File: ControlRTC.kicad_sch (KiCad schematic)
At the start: 28 parts, among them M1 Fan_4pin, SW1 SW_USER, SW2 SW_WIPE, U18 74LVC1G07, U19 74LVC1G07, U20 LP5569RTWR, U21 PCF85063AT, Y2 X32K768S301

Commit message: Use impedance for JLC7628 stackup/switch HDMI/SW2 placement
Use JLC7628 impedance values to get more options in color selection.
Also this leads to slightly wider traces typically, and it will be
easier to switch back to JLC2313 or the like than the other way around.

Also swap placing of HDMI/SW2 and rotate the heatsink by 90° for easier
routing.

Signed-off-by: Stefan Agner <stefan@agner.ch>
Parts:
- SW1: footprint Button_Switch_THT:SW_Tactile_SPST_Angled_PTS645Vx58-2LFS -> Button_Switch_THT:SW_Tactile_SPST_Angled_PTS645Vx83-2LFS; PartNumber PTS645VM58-2 LFS -> PTS645VM83-2 LFS
- SW2: footprint Button_Switch_THT:SW_Tactile_SPST_Angled_PTS645Vx39-2LFS -> Button_Switch_THT:SW_Tactile_SPST_Angled_PTS645Vx58-2LFS; PartNumber PTS645VK39-2 LFS -> PTS645VK58-2 LFS
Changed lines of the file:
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@@
     (property "Reference" "SW1" (id 0) (at 60.325 39.37 0))
     (property "Value" "SW_USER" (id 1) (at 60.325 41.91 0))
-    (property "Footprint" "Button_Switch_THT:SW_Tactile_SPST_Angled_PTS645Vx58-2LFS" (id 2) (at 59.69 46.355 0)
+    (property "Footprint" "Button_Switch_THT:SW_Tactile_SPST_Angled_PTS645Vx83-2LFS" (id 2) (at 59.69 46.355 0)
       (effects (font (size 1.27 1.27)) hide)
     )
@@
       (effects (font (size 1.27 1.27)) hide)
     )
-    (property "PartNumber" "PTS645VM58-2 LFS" (id 5) (at 59.69 46.355 0)
+    (property "PartNumber" "PTS645VM83-2 LFS" (id 5) (at 59.69 46.355 0)
       (effects (font (size 1.27 1.27)) hide)
     )
@@
     (property "Reference" "SW2" (id 0) (at 102.235 39.37 0))
     (property "Value" "SW_WIPE" (id 1) (at 102.235 41.91 0))
-    (property "Footprint" "Button_Switch_THT:SW_Tactile_SPST_Angled_PTS645Vx39-2LFS" (id 2) (at 101.6 46.355 0)
+    (property "Footprint" "Button_Switch_THT:SW_Tactile_SPST_Angled_PTS645Vx58-2LFS" (id 2) (at 101.6 46.355 0)
       (effects (font (size 1.27 1.27)) hide)
     )
@@
       (effects (font (size 1.27 1.27)) hide)
     )
-    (property "PartNumber" "PTS645VK39-2 LFS" (id 5) (at 101.6 46.355 0)
+    (property "PartNumber" "PTS645VK58-2 LFS" (id 5) (at 101.6 46.355 0)
       (effects (font (size 1.27 1.27)) hide)
     )

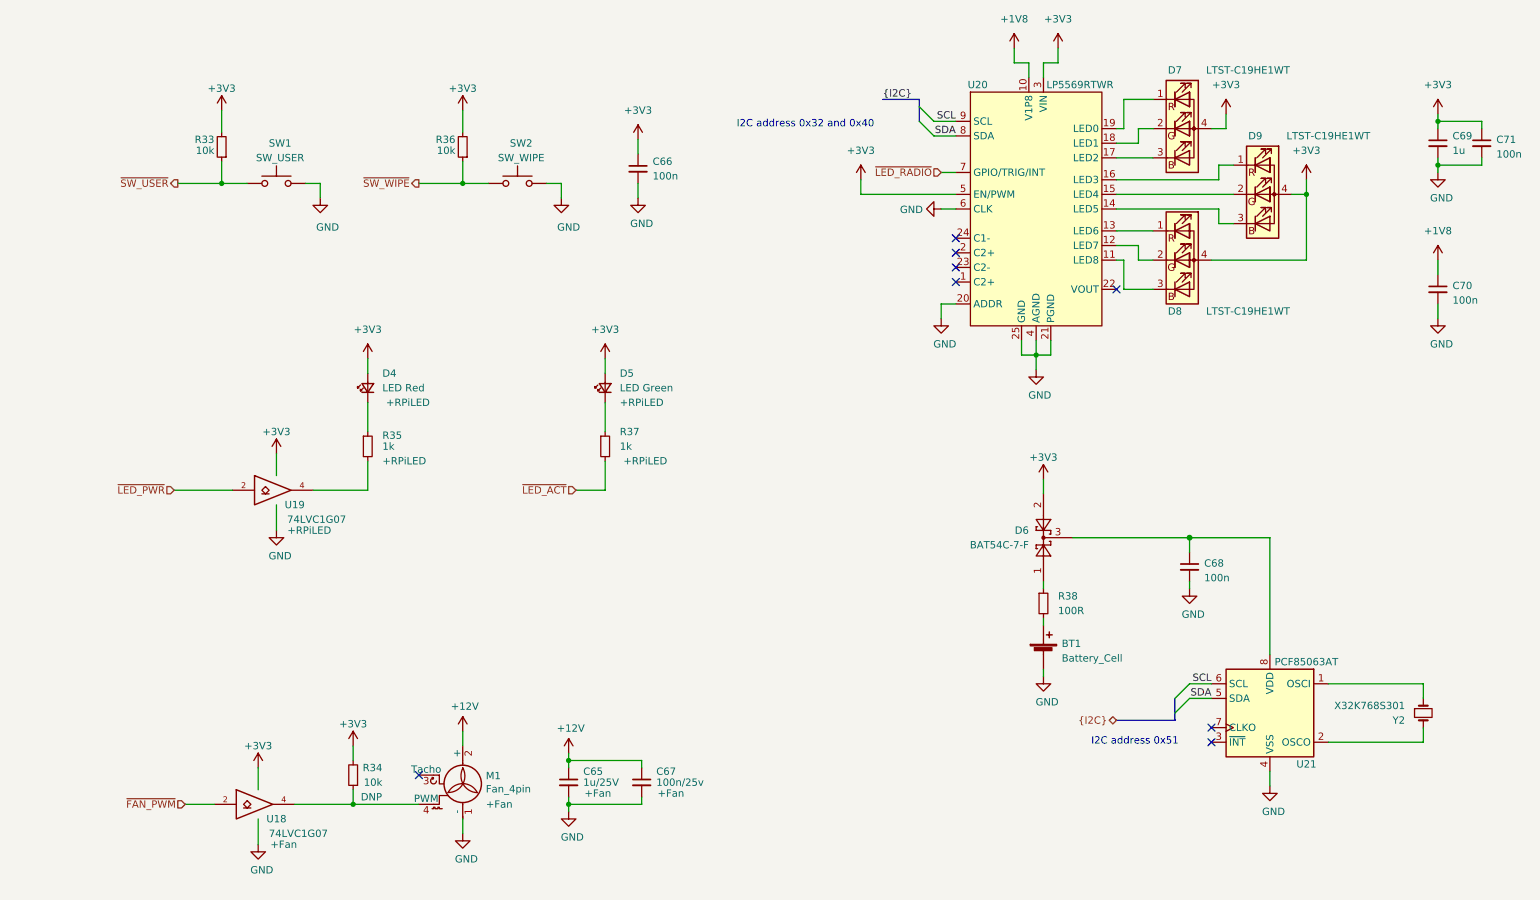
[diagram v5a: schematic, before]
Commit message: pcb 0.2:
Changes:
Footrints:
-Modified DC Jack to accomodate CUI PJ-002A
-Modified RJ45 to increase clearance between shield and poe pins
-Modified m.2 mounting pads to avoid drc errors
Schematic:
-usb-c facing usb mux is supplied by +3v3VP
-added misc. capacitors
PCB
-min. annular ring for vias set to 0.125 from 0.2

Signed-off-by: Dominik Sliwa <dominik@sliwa.io>
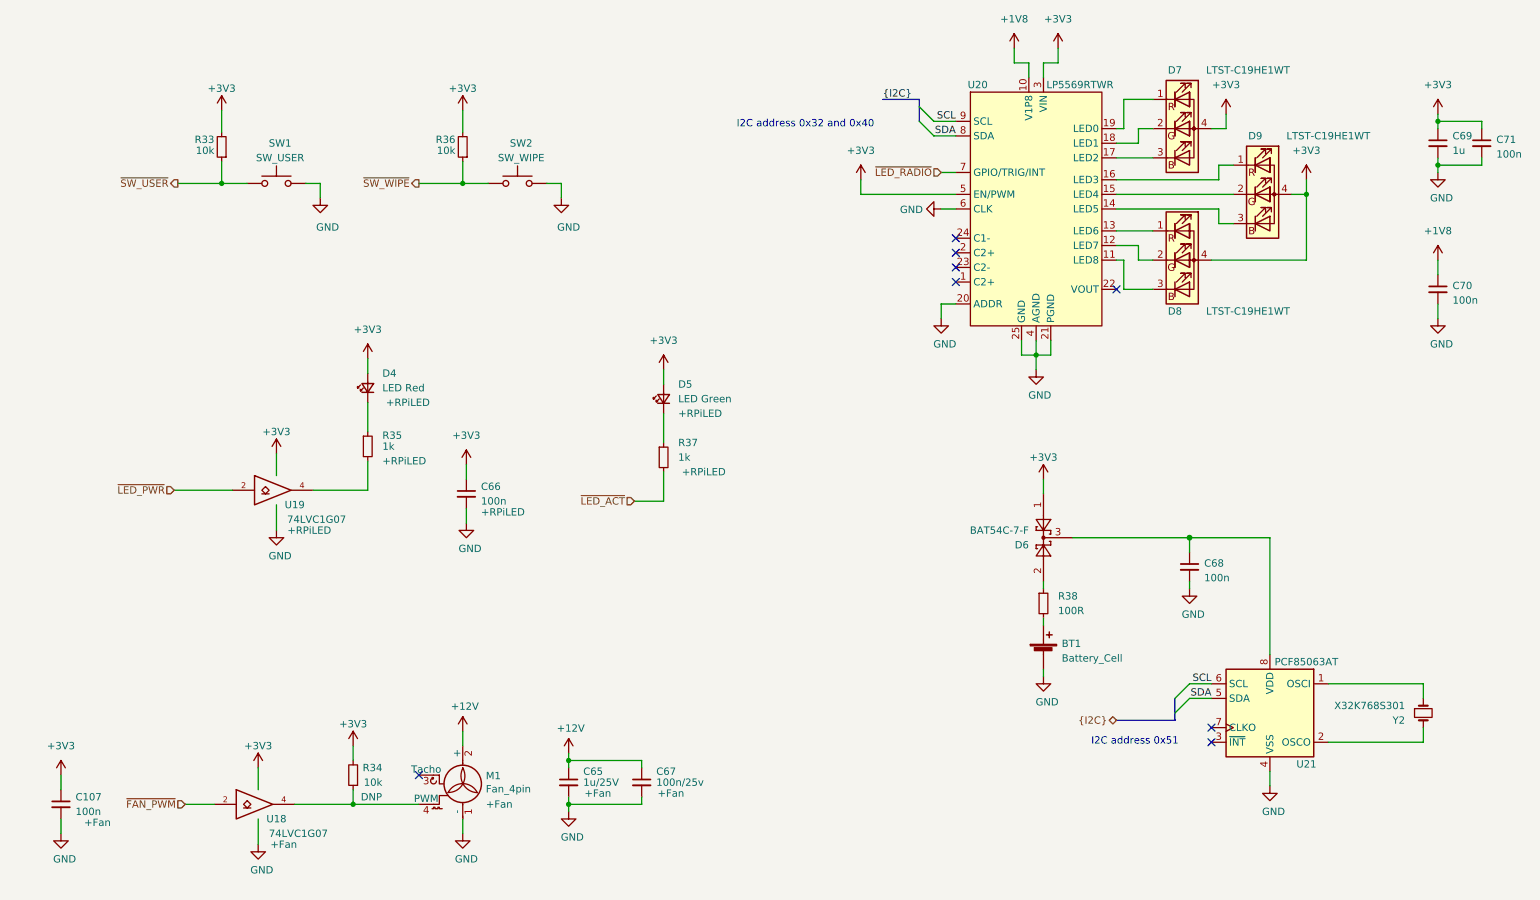
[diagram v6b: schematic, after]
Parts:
- added C107: 100n, Capacitor_SMD:C_0402_1005Metric, symbol Device:C_Small
- C66: Config (none) -> +RPiLED
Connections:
- net +3V3: now also D6.1, C107.1; no longer D6.2
- net GND: now also C107.2
- net at R38.1: now also D6.2; no longer D6.1
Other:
- moved on the sheet: C66, D5, R37

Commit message: initial rev 0.3:
updates
schematic:
-change usb current protection IC to 1.5A
-Added low-pass filter to the audio output
-PoE fixed primary windings polarity
-added option to select poe class with a jumper (between 3 and 4)
-fixes in poe design
-added testpoints
-added virtual hirose df40c connectors for pick and place use

lightblue.pretty:
-added fake DF40C footprint for pick and place and 3d model purposes

Signed-off-by: Dominik Sliwa <dominik@sliwa.io>
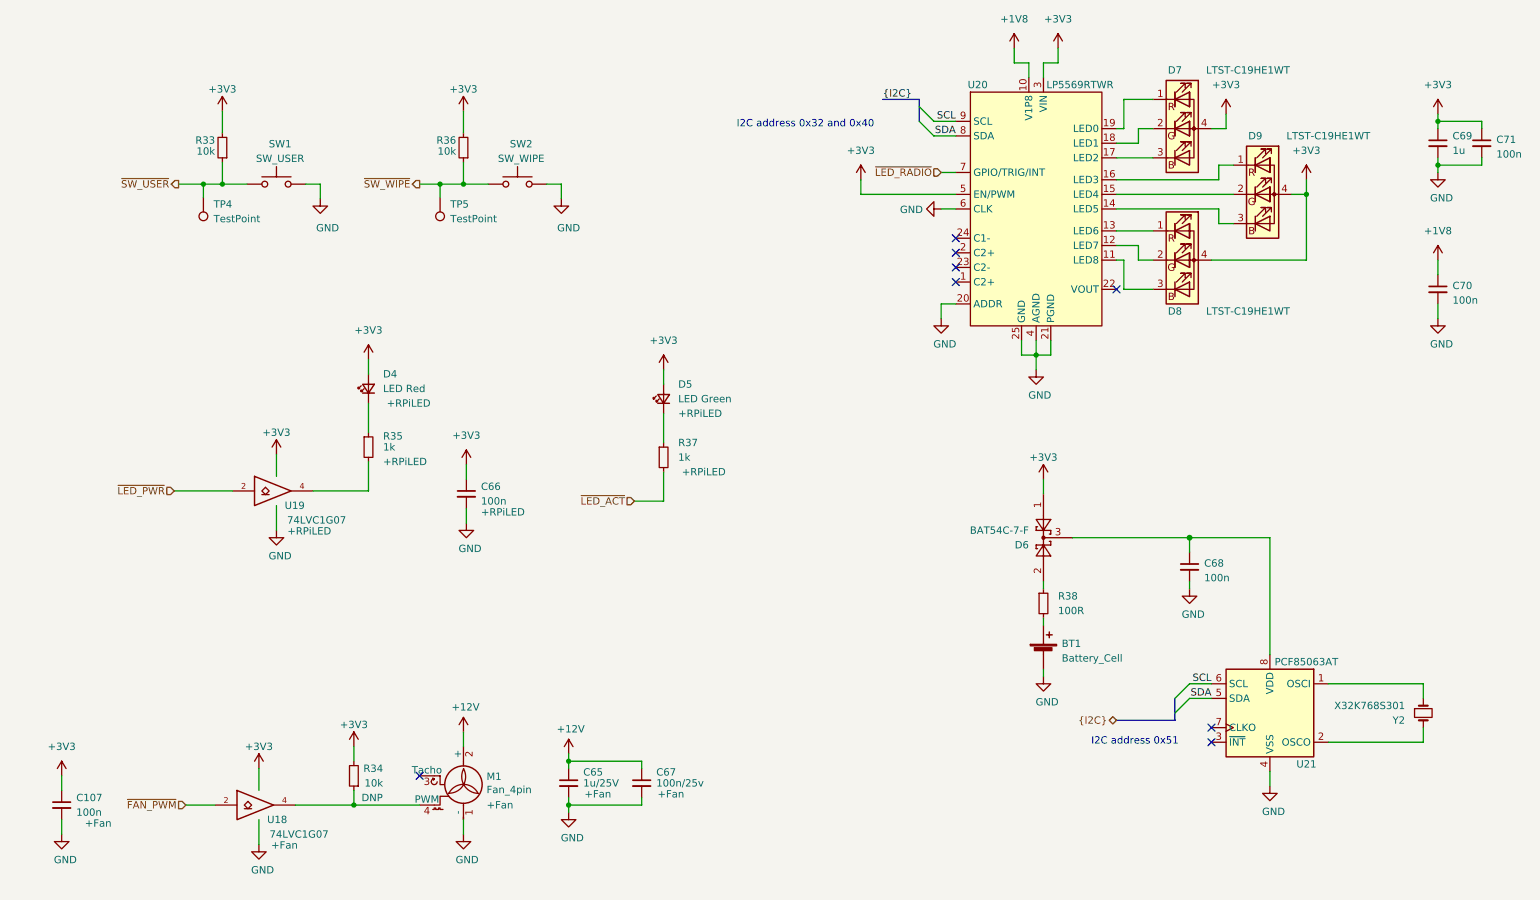
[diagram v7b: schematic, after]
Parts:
- added TP4, TP5: TestPoint, TestPoint:TestPoint_Pad_D1.0mm, symbol Connector:TestPoint
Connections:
- net ~SW_USER: now also TP4.1
- net ~SW_WIPE: now also TP5.1

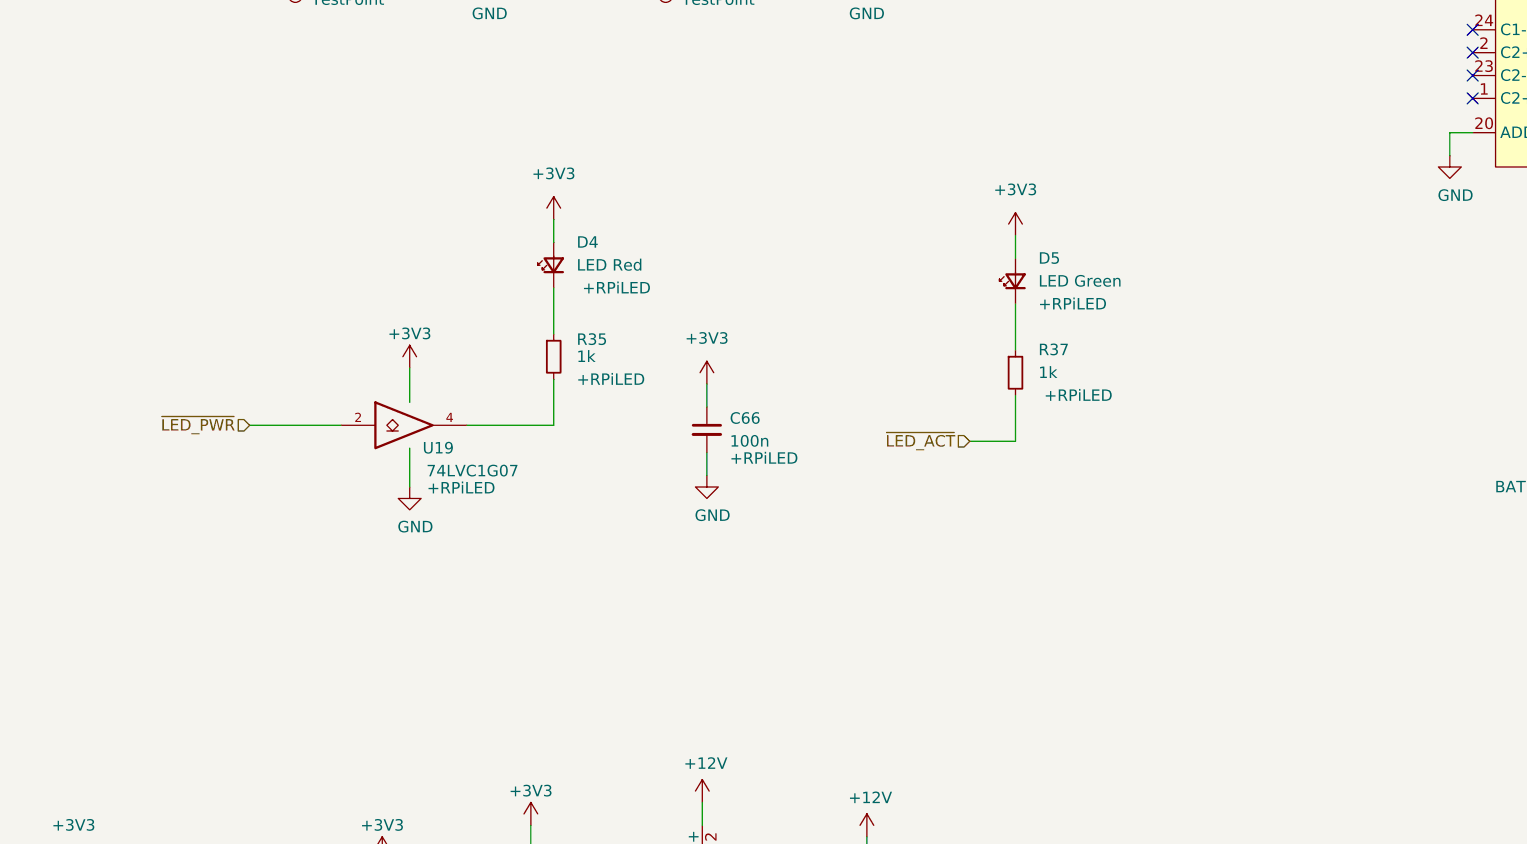
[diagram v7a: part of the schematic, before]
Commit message: Add test points for I2C
Signed-off-by: Stefan Agner <stefan@agner.ch>
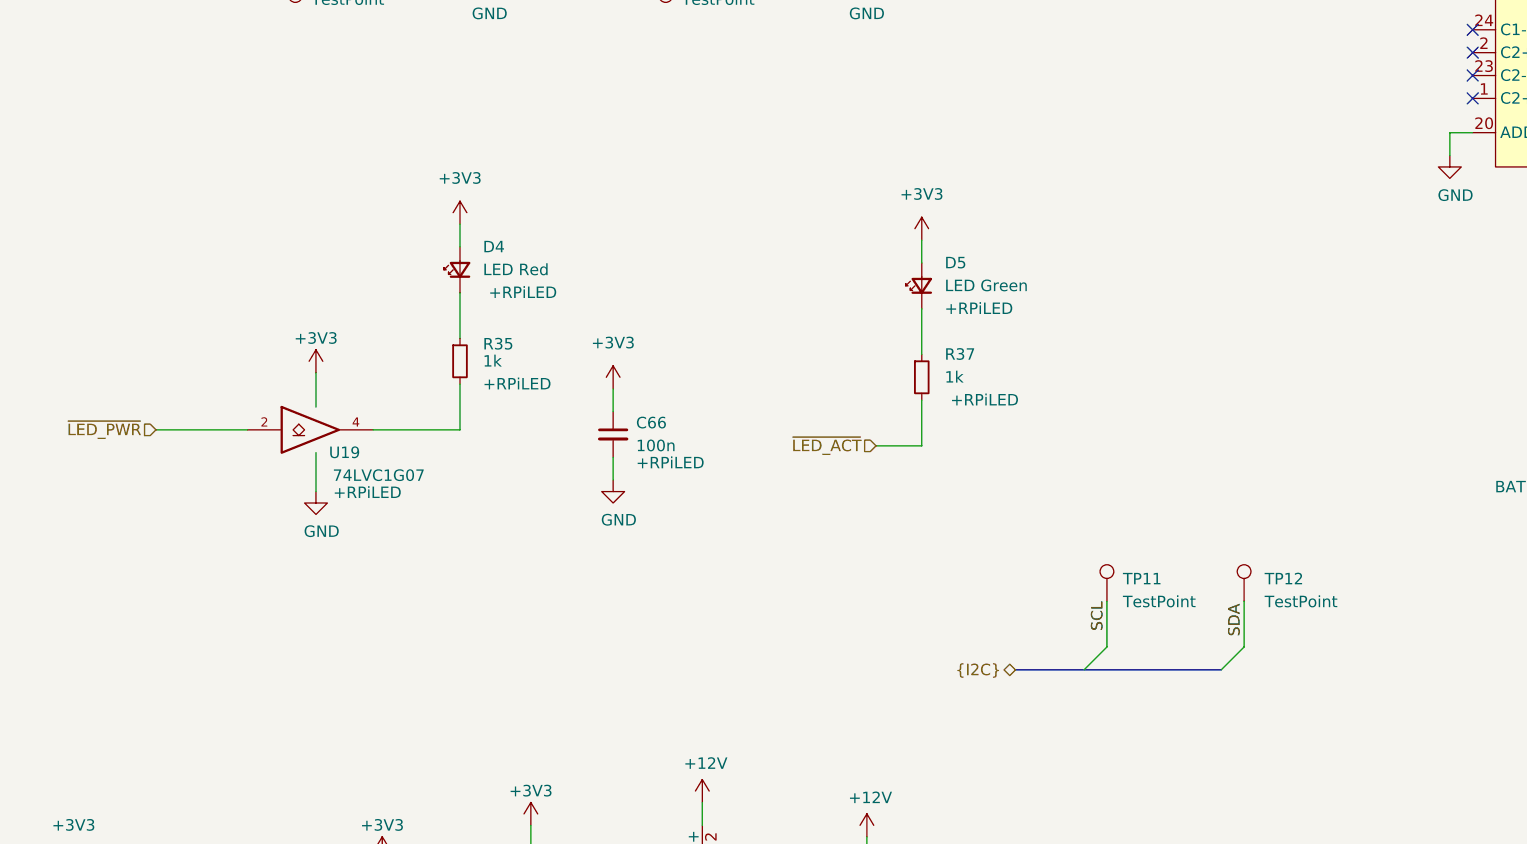
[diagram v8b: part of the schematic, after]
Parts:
- added TP11, TP12: TestPoint, TestPoint:TestPoint_Pad_D1.0mm, symbol Connector:TestPoint
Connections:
- net SCL: now also TP11.1
- net SDA: now also TP12.1
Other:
- moved on the sheet: C66, D4, D5, R35, R37, U19
